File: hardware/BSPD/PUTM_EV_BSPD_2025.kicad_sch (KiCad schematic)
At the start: 37 parts, among them J1 BS2, J2 BS1, J3 CS, K2 TE AXICOM IM07DTS, Q1 BS170F, U10 LM393B, U11 74HC1G08GV, U3 74HC2G14-Q100, U5 74HC1G08GV, U8 NE555DR

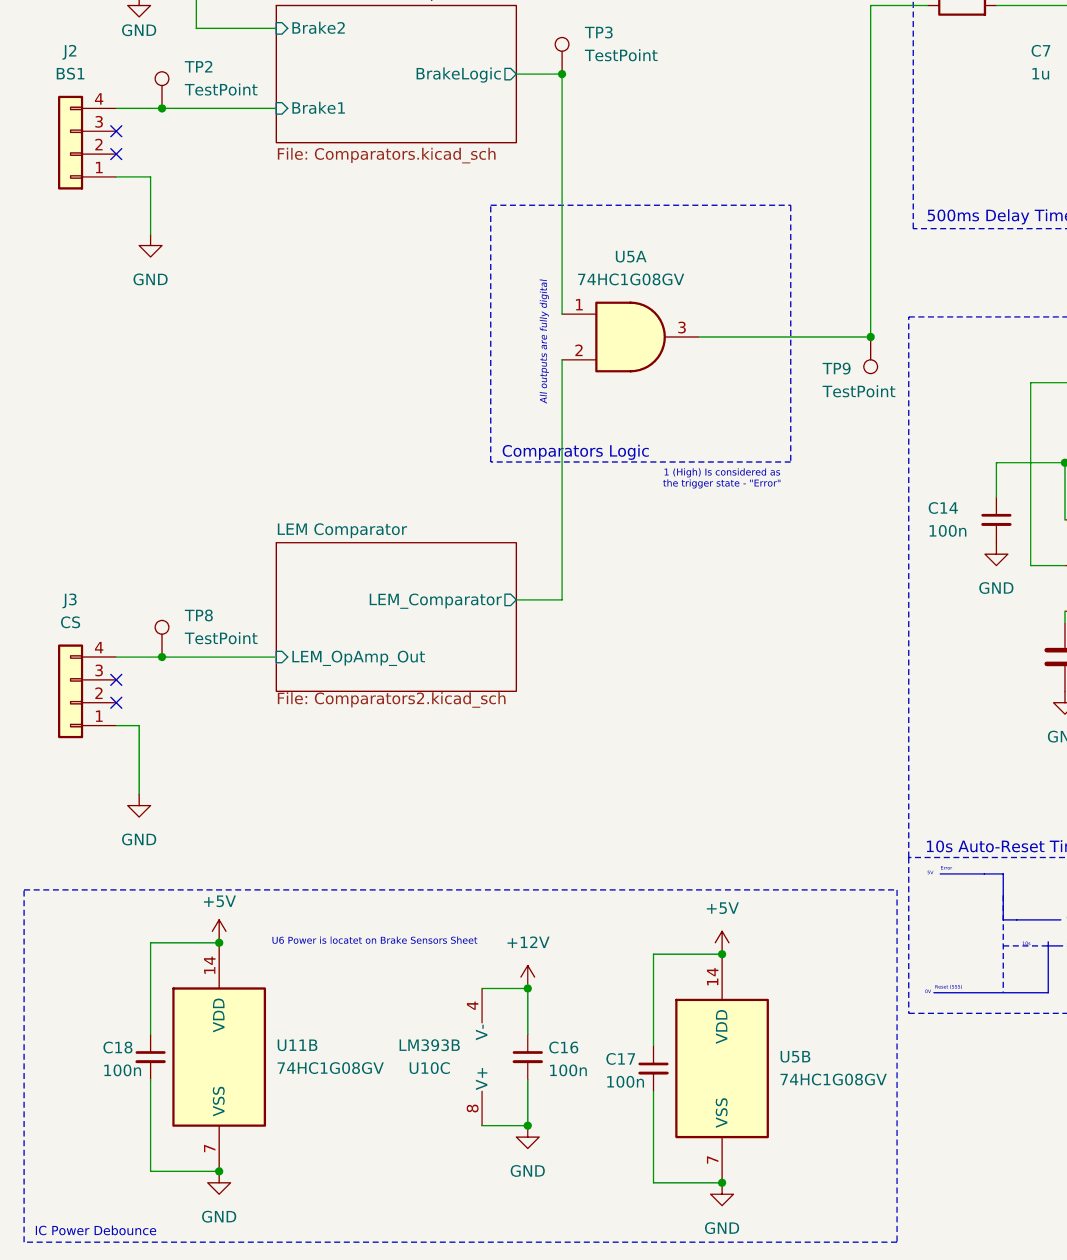
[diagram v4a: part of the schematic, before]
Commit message: Fixed schematic symbol errors
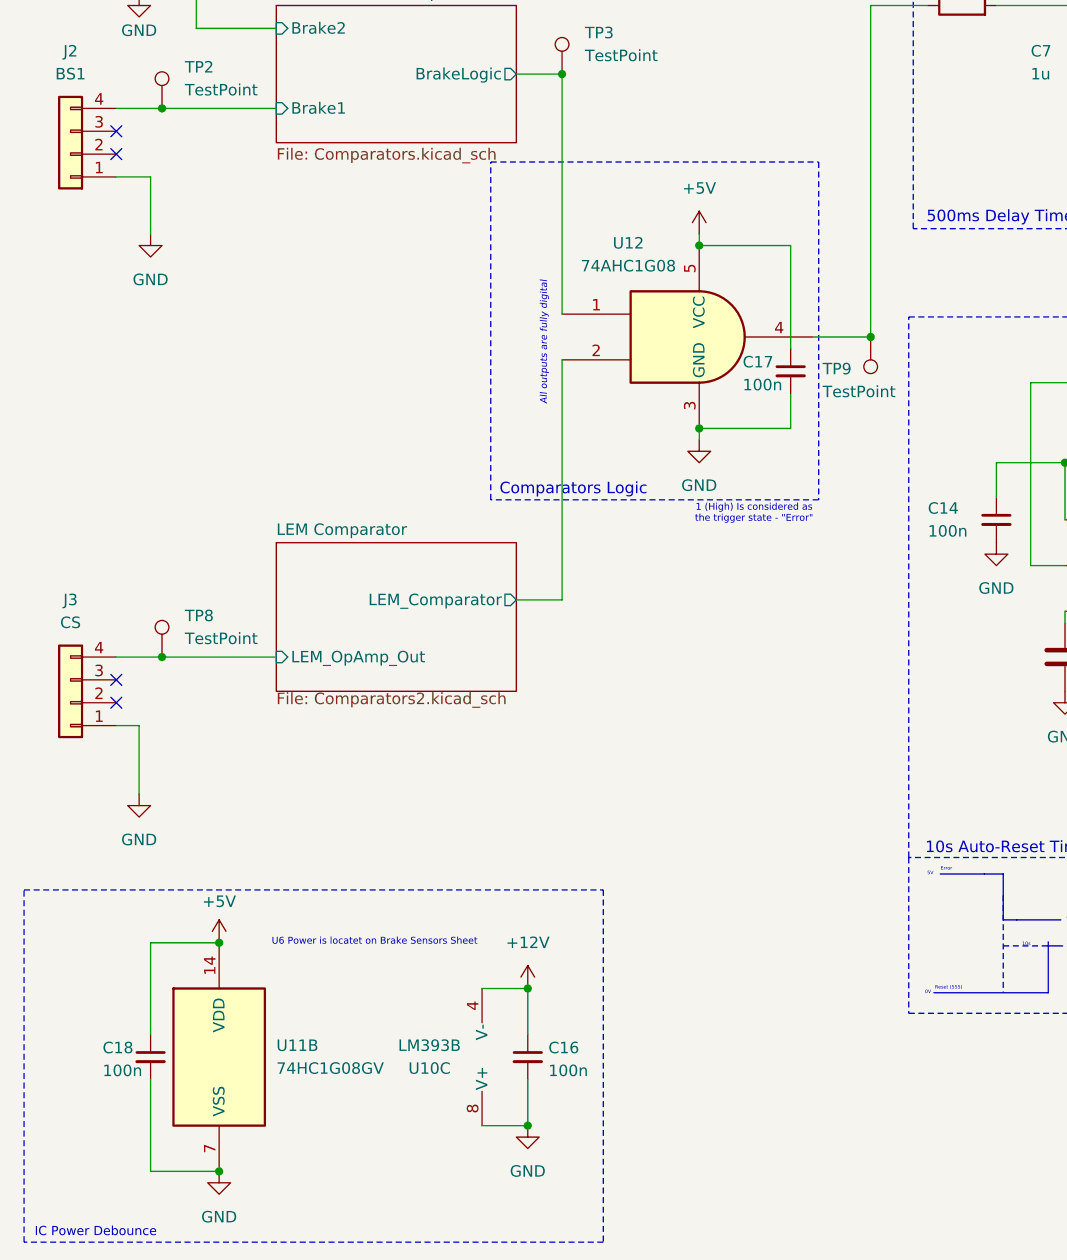
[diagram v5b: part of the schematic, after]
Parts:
- removed U5: 74HC1G08GV, Package_TO_SOT_SMD:SC-74A-5_1.55x2.9mm_P0.95mm, symbol 4xxx:4081
- added unit 1 of U11
- added U12: 74AHC1G08, symbol 74xGxx:74AHC1G08
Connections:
- net +5V: now also U12.5 (VCC)
- net Brake Sensors Comparators/BrakeLogic: now also U12.1
- net GND: now also U12.3 (GND)
- net LEM Comparator/LEM_Comparator: now also U12.2
- net at Q1.2 (G), R20.1, TP12.1: now also U11.3; no longer U11.3
- net at R18.1, TP9.1: now also U12.4
- net at U3.6: now also U11.1; no longer U11.1
- net at TP11.1, U8.3 (Q): now also U11.2; no longer U11.2
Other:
- moved on the sheet: C17

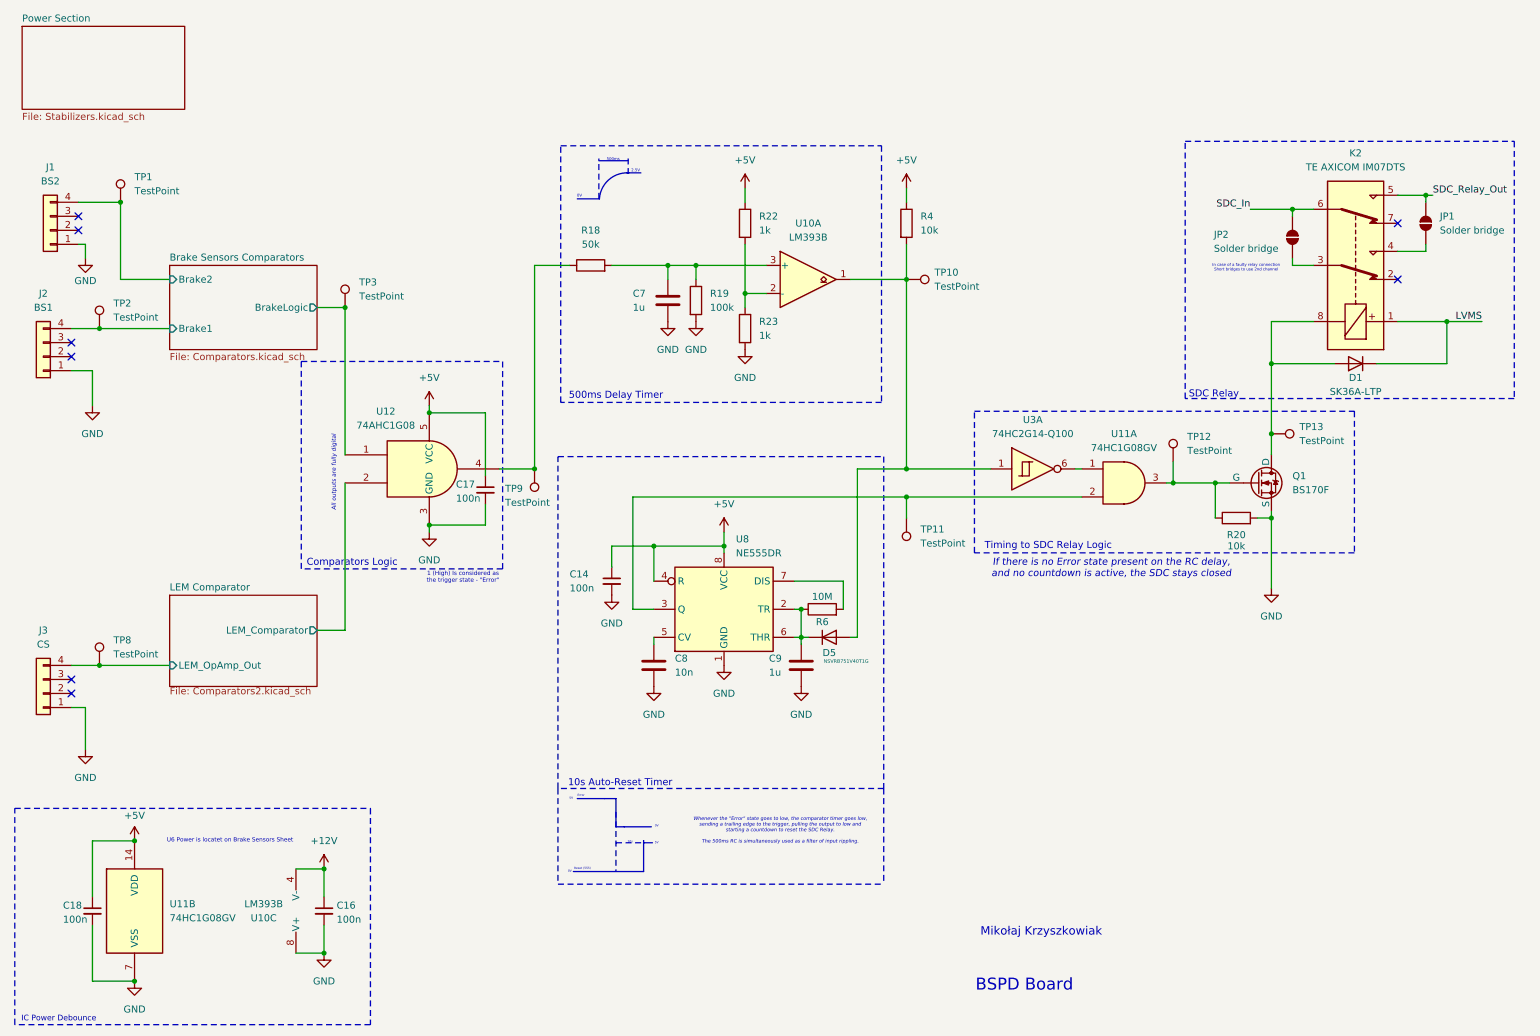
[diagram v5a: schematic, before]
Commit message: Layout and connections added
First version of board layout and connections added, to be checked and improved 

I know about 4 DRC errors, I will fix them, but that is what i have for now
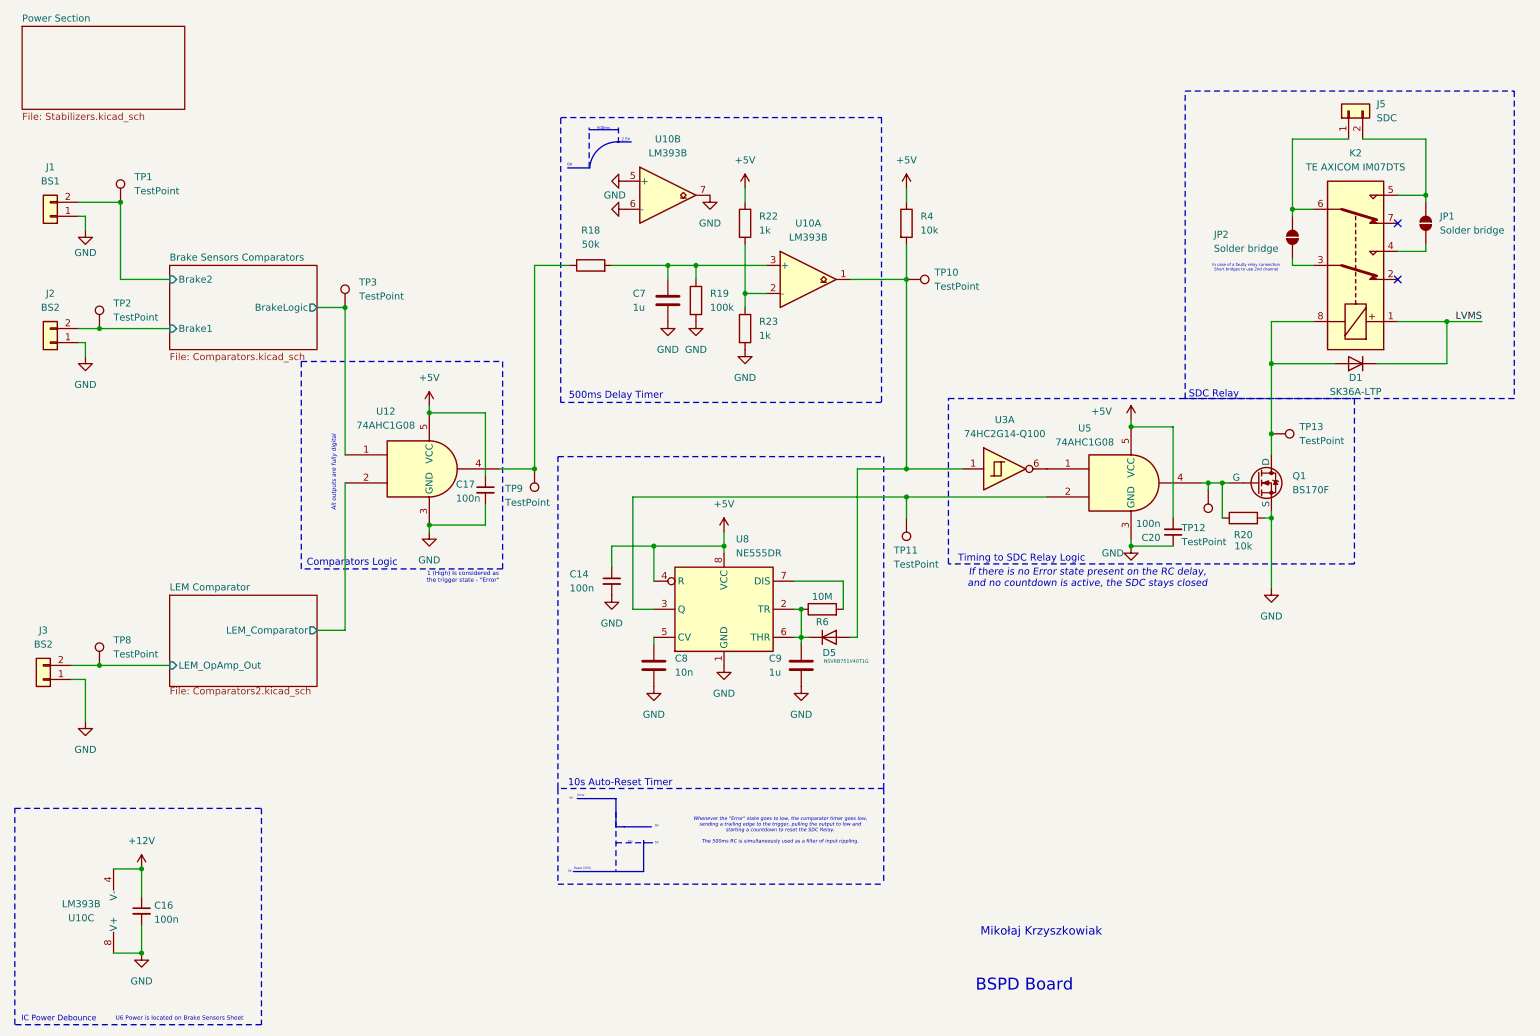
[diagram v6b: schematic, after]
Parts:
- removed C18: 100n, Capacitor_SMD:C_0603_1608Metric, symbol Device:C_Small
- removed J1: BS2, symbol Connector_Generic:Conn_01x04
- removed J2: BS1, symbol Connector_Generic:Conn_01x04
- removed J3: CS, symbol Connector_Generic:Conn_01x04
- removed U11: 74HC1G08GV, Package_TO_SOT_SMD:SC-74A-5_1.55x2.9mm_P0.95mm, symbol 4xxx:4081
- added C20: 100n, Capacitor_SMD:C_0603_1608Metric, symbol Device:C_Small
- added J1: BS1, Connector_Wire:SolderWire-0.1sqmm_1x02_P3.6mm_D0.4mm_OD1mm_Relief, symbol Connector_Generic:Conn_01x02
- added J2, J3: BS2, Connector_Wire:SolderWire-0.1sqmm_1x02_P3.6mm_D0.4mm_OD1mm_Relief, symbol Connector_Generic:Conn_01x02
- added J5: SDC, Connector_Wire:SolderWire-0.1sqmm_1x02_P3.6mm_D0.4mm_OD1mm_Relief, symbol Connector_Generic:Conn_01x02
- added unit 3 of U10
- added U5: 74AHC1G08, Package_TO_SOT_SMD:SC-74A-5_1.55x2.9mm_P0.95mm, symbol 74xGxx:74AHC1G08
- C14: footprint (none) -> Capacitor_SMD:C_0603_1608Metric
- JP1, JP2: footprint (none) -> Jumper:SolderJumper-2_P1.3mm_Open_RoundedPad1.0x1.5mm
- TP1, TP10, TP11, TP12, TP13, TP2, TP3, TP8, TP9: footprint (none) -> TestPoint:TestPoint_Pad_D1.0mm
- U12: footprint (none) -> Package_TO_SOT_SMD:SC-74A-5_1.55x2.9mm_P0.95mm
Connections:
- net +12V: now also U10.4 (V-); no longer U10.4 (V-)
- net +5V: now also C20.2, U5.5 (VCC)
- net Brake Sensors Comparators/Brake1: now also J2.2 (Pin_2)
- net Brake Sensors Comparators/Brake2: now also J1.2 (Pin_2)
- net GND: now also U10.5 (+), U10.6 (-), U10.7, C20.1, J1.1 (Pin_1), J2.1 (Pin_1), J3.1 (Pin_1), U10.8 (V+), U5.3 (GND); no longer U10.8 (V+)
- net LEM Comparator/LEM_OpAmp_Out: now also J3.2 (Pin_2)
- net at R22.2, R23.1: now also U10.2 (-); no longer U10.2 (-)
- net at Q1.2 (G), R20.1, TP12.1: now also U5.4
- net at C7.1, R18.2, R19.1: now also U10.3 (+); no longer U10.3 (+)
- net at D5.2 (A), R4.2, TP10.1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: now also U10.1; no longer U10.1
- net at U3.6: now also U5.1
- net at TP11.1, U8.3 (Q): now also U5.2
- net SDC_In: no longer names the net of JP2.2 (B), K2.6
- net SDC_In: now also J5.1 (Pin_1)
- net SDC_Relay_Out: no longer names the net of JP1.2 (B), K2.5
- net SDC_Relay_Out: now also J5.2 (Pin_2)
- no-connect marks 8 -> 2
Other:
- note added: "U6 Power is located on Brake Sensors Sheet"
- note removed: "U6 Power is locatet on Brake Sensors Sheet"
- moved on the sheet: C16, R20, TP12, U10B, U3A

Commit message: Minor footprint changes + fixed DRC errors
Fixed all critical DRC errors and minor warnings; warnings that were not important/valid have been excluded.

Switched wire holes (in Strain Relief footprint) to 0.4mm from 0.1mm to match 22AWG wire size.
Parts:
- J1, J2, J3, J5: footprint Connector_Wire:SolderWire-0.1sqmm_1x02_P3.6mm_D0.4mm_OD1mm_Relief -> Connector_Wire:SolderWire-0.5sqmm_1x02_P3.6mm_D0.5mm_OD1mm_Relief
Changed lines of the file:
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@@
 			)
 		)
-		(property "Footprint" "Connector_Wire:SolderWire-0.1sqmm_1x02_P3.6mm_D0.4mm_OD1mm_Relief"
+		(property "Footprint" "Connector_Wire:SolderWire-0.5sqmm_1x02_P3.6mm_D0.5mm_OD1mm_Relief"
 			(at 254 31.75 0)
 			(effects
@@
 			)
 		)
-		(property "Footprint" "Connector_Wire:SolderWire-0.1sqmm_1x02_P3.6mm_D0.4mm_OD1mm_Relief"
+		(property "Footprint" "Connector_Wire:SolderWire-0.5sqmm_1x02_P3.6mm_D0.5mm_OD1mm_Relief"
 			(at 19.05 50.8 0)
 			(effects
@@
 			)
 		)
-		(property "Footprint" "Connector_Wire:SolderWire-0.1sqmm_1x02_P3.6mm_D0.4mm_OD1mm_Relief"
+		(property "Footprint" "Connector_Wire:SolderWire-0.5sqmm_1x02_P3.6mm_D0.5mm_OD1mm_Relief"
 			(at 17.78 134.62 0)
 			(effects
@@
 			)
 		)
-		(property "Footprint" "Connector_Wire:SolderWire-0.1sqmm_1x02_P3.6mm_D0.4mm_OD1mm_Relief"
+		(property "Footprint" "Connector_Wire:SolderWire-0.5sqmm_1x02_P3.6mm_D0.5mm_OD1mm_Relief"
 			(at 19.05 73.66 0)
 			(effects

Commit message: Major changes. Read ext. description.
- Changed board to 4 layers due to trace fitment issues (or skill issues)
- Added mounting holes to be compatible with previous gen. of board
- Added unassigned footprints
- Fully fixed DRC errors
- Fixed comp. issues with schematic
- Added missing custom footprints to library (and made the library)
NOTE: Ignore "not matching with library copy" - It's matching. Trust me.
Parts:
- J1, J2, J3, J5: footprint Connector_Wire:SolderWire-0.5sqmm_1x02_P3.6mm_D0.5mm_OD1mm_Relief -> footprints:Wire_StrainRelief
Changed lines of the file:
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@@
 			)
 		)
-		(property "Footprint" "Connector_Wire:SolderWire-0.5sqmm_1x02_P3.6mm_D0.5mm_OD1mm_Relief"
+		(property "Footprint" "footprints:Wire_StrainRelief"
 			(at 254 31.75 0)
 			(effects
@@
 			)
 		)
-		(property "Footprint" "Connector_Wire:SolderWire-0.5sqmm_1x02_P3.6mm_D0.5mm_OD1mm_Relief"
+		(property "Footprint" "footprints:Wire_StrainRelief"
 			(at 19.05 50.8 0)
 			(effects
@@
 			)
 		)
-		(property "Footprint" "Connector_Wire:SolderWire-0.5sqmm_1x02_P3.6mm_D0.5mm_OD1mm_Relief"
+		(property "Footprint" "footprints:Wire_StrainRelief"
 			(at 17.78 134.62 0)
 			(effects
@@
 			)
 		)
-		(property "Footprint" "Connector_Wire:SolderWire-0.5sqmm_1x02_P3.6mm_D0.5mm_OD1mm_Relief"
+		(property "Footprint" "footprints:Wire_StrainRelief"
 			(at 19.05 73.66 0)
 			(effects
